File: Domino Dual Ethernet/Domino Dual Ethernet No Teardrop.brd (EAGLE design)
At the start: 38.1 x 30.5 mm, 29 parts, among them J1 MH10-1, J2 B50(27-51)FP4-151-A613-B12, J3 B50(27-51)FP4-151-A613-B12, J4 FR04-2, J5 FR04-1

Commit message: Changed copyright
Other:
- board text added: "Reference designs are provided "AS IS" and "WITH ALL FAULTS". The Domino Team disclaims all other warranties express or implied, regarding this product, including but not limited to, any implied warranties of merchantibility or fitness for any particular application."
- board text added: "The Domino Team may make changes to specifications and product descriptions at any time, without notice."
- board text added: "© 2014, The Domino Team. All rights reserved."
- board text removed: "Michel Stempin may make changes to specifications and product descriptions at any time, without notice."
- board text removed: "Reference designs are provided "AS IS" and "WITH ALL FAULTS". Michel Stempin disclaims all other warranties express or implied, regarding this product, including but not limited to, any implied warranties of merchantibility or fitness for any particular application."
- board text removed: "© 2014, Michel Stempin. All rights reserved."
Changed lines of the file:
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@@
 See creativecommons.org/licenses/by-sa/4.0/</text>
 <text x="34.29" y="-51.943" size="0.8128" layer="48" ratio="20">Reference designs are provided "AS IS" and "WITH ALL FAULTS".
-Michel Stempin disclaims all other warranties express or implied,
+The Domino Team disclaims all other warranties express or implied,
 regarding this product, including but not limited to, any implied warranties of
 merchantibility or fitness for any particular application.</text>
-<text x="34.29" y="-55.753" size="0.8128" layer="48" ratio="20">Michel Stempin may make changes to specifications and product descriptions
+<text x="34.29" y="-55.753" size="0.8128" layer="48" ratio="20">The Domino Team may make changes to specifications and product descriptions
 at any time, without notice.</text>
-<text x="74.93" y="-41.91" size="1.27" layer="48" ratio="20">© 2014, Michel Stempin.
+<text x="74.93" y="-41.91" size="1.27" layer="48" ratio="20">© 2014, The Domino Team.
 All rights reserved.</text>
 <text x="115.57" y="-57.15" size="1.778" layer="48">Rev.</text>

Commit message: Domino tile Dual Ethernet Revision B
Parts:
- removed J4: FR04-2, Domino:FR04-2-0.1
- removed J5: FR04-1, Domino:FR04-1-0.1
- added D1: BLUE, Domino:LED0603
- added D2: WHITE, Domino:LED0603
- added D3, D4, D5, D6: GREEN, Domino:LED0603
- added D7: RED, Domino:LED0603
- added D8: ORANGE, Domino:LED0603
- added D9: YELLOW, Domino:LED0603
- added R10, R11, R12, R13, R15: 270R, Domino:R0603
- added R14, R16: 150R, Domino:R0603
- added R17, R18: 330R, Domino:R0603
- added R9: 49R9, Domino:R0402
- added U$13: (no value), Domino:DOMINO_LOGO_SMALL
- added U$16: (no value), Domino:OPEN_HARDWARE_LOGO
- C1: device Domino:C1210 -> Domino:C1206
- J1: value MH10-1 -> B59(57-02)F4-03-1212-C12; device Domino:MH10-1-0.1 -> Domino:B59(57-02)F4-03-1212-C12
- J2, J3: value B50(27-51)FP4-151-A613-B12 -> MH18-1; device Domino:B50(27-51)FP4-151-A613-B12 -> Domino:MH18-1-0.1
- R1: value 49R9 -> 330R; device Domino:R0402 -> Domino:R0603
- moved J2 36.4 mm to (1.27, 31.8), flipped to the bottom, turned to 180 degrees
- moved U$4 32.8 mm to (39.4, 14.6), flipped to the bottom, turned to 270 degrees
- moved C5 26.3 mm to (29.0, 11.3), turned to 90 degrees
- moved R7 24.1 mm to (27.4, 22.1), flipped to the top
- moved R8 22.1 mm to (27.4, 17.7), flipped to the top, turned to 180 degrees
- moved U$7 22.1 mm to (30.5, 12.7)
- moved C6 21.5 mm to (29.0, 21.6), flipped to the top, turned to 270 degrees
- moved U$6 21.0 mm to (9.53, 3.17)
- moved C3 20.2 mm to (18.1, 5.32), flipped to the top, turned to 90 degrees
- moved U$8 19.3 mm to (15.9, 22.2)
- moved R5 18.5 mm to (27.4, 11.8), turned to 180 degrees
- moved C4 17.9 mm to (29.0, 14.7), flipped to the top
- moved U$5 14.5 mm to (17.8, 3.17)
- moved R6 14.4 mm to (27.4, 21.1)
- moved C1 14.3 mm to (15.5, 27.8), flipped to the top, turned to 180 degrees
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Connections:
- removed net P0_LED_L_A: J2.13, J4.8
- removed net P0_LED_L_C: J2.14, J4.7
- removed net P0_LED_R_A: J2.11, J4.4
- removed net P0_LED_R_C: J2.12, J4.3
- removed net P4_LED_L_A: J3.13, J4.6
- removed net P4_LED_L_C: J3.14, J4.5
- removed net P4_LED_R_A: J3.11, J4.2
- removed net P4_LED_R_C: J3.12, J4.1
- removed net VC12: J3.9, J5.3
- removed net VC36: J3.10, J5.4
- removed net VC45: J3.4, J5.1
- removed net VC78: J3.5, J5.2
- new net +3V3: D7.2, D8.2, D9.2, J1.UL2, J2.8, R1.2
- new net LAN1_LED: D3.2, R12.2
- new net LAN2_LED: D4.2, R13.2
- new net LAN3_LED: D5.2, J1.DL2, R14.2
- new net LAN4_LED: D6.2, R15.2
- new net LED0: J2.9, R10.1
- new net LED1: J2.10, R11.1
- new net LED2: J2.11, R12.1
- new net LED3: J2.12, R13.1
- new net LED4: J2.13, R14.1
- new net LED5: J2.14, R15.1
- new net LED6: J2.15, R16.1
- new net LED7: J2.16, R17.1
- new net LED8: J2.17, R18.1
- new net POWER_LED: J1.DL4, J1.UL4, R1.1
- new net SYS_LED: D8.1, R17.2
- new net USB_LED: D2.2, R11.2
- new net WAN_LED: D7.1, J1.UL1, R16.2
- new net WLAN_LED: D1.2, R10.2
- new net WPS_LED: D9.1, R18.2
- net +2VA_ETH_OUT: now also C2.2, C3.2, J1.DR2, J1.DR5, J1.UR2, J1.UR5, J3.14; no longer C6.2, C7.2, J1.6, J2.3, J3.3
- net GND: now also D1.1, D2.1, D3.1, D4.1, D5.1, D6.1, J1.DL1, J1.DL3, J1.UL3, J2.18, J3.9; no longer J1.1
- net P0_RX: now also C7.2, R8.1, R9.1; no longer C2.2, R1.1, R2.1
- net P0_RX_N: now also J1.DR3, J3.16, R9.2; no longer J1.8, J2.2, R2.2
- net P0_RX_P: now also J1.DR1, J3.15, R8.2; no longer J1.7, J2.1, R1.2
- net P0_TX: now also C6.2, R6.1, R7.1; no longer C3.2, R3.1, R4.1
- net P0_TX_N: now also J1.DR6, J3.18, R7.2; no longer J1.10, J2.8, R4.2
- net P0_TX_P: now also J1.DR4, J3.17, R6.2; no longer J1.9, J2.7, R3.2
- net P4_RX: now also C5.2, R4.1; no longer C4.2, R6.1
- net P4_RX_N: now also J1.UR6, J3.11, R5.2; no longer J1.3, J3.8, R6.2
- net P4_RX_P: now also J1.UR4, J3.10, R4.2; no longer J1.2, J3.7, R5.2
- net P4_TX: now also C4.2, R2.1, R3.1; no longer C5.2, R7.1, R8.1
- net P4_TX_N: now also J1.UR3, J3.13, R3.2; no longer J1.5, J3.2, R8.2
- net P4_TX_P: now also J1.UR1, J3.12, R2.2; no longer J1.4, J3.1, R7.2
- net SHIELD: now also J1.DR8, J1.P$1, J1.P$2, J1.P$3, J1.P$4, J1.UR8; no longer J2.6, J2.SH$1, J2.SH$2, J3.6, J3.SH$1, J3.SH$2
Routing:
- net +3V3: track 0.00 -> 56.1 mm, vias 0 -> 2
- net P4_LED_R_A: track 52.3 -> 0.00 mm
- net WAN_LED: track 0.00 -> 51.6 mm, vias 0 -> 1
- net P4_LED_R_C: track 47.2 -> 0.00 mm
- net LAN3_LED: track 0.00 -> 43.5 mm, vias 0 -> 1
- net P4_LED_L_A: track 41.9 -> 0.00 mm
- net P4_LED_L_C: track 36.5 -> 0.00 mm
- net +2VA_ETH_OUT: track 37.7 -> 74.0 mm
- net GND: track 0.00 -> 34.2 mm, vias 31 -> 57
- net P0_LED_R_A: track 32.3 -> 0.00 mm
- net POWER_LED: track 0.00 -> 31.1 mm, vias 0 -> 1
- net P0_LED_L_A: track 26.8 -> 0.00 mm
- net P0_LED_R_C: track 26.4 -> 0.00 mm
- net P0_TX_N: track 20.6 -> 47.0 mm, vias 0 -> 1
- net P0_LED_L_C: track 23.3 -> 0.00 mm
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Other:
- board size 38.1 x 30.5 mm -> 45.7 x 33 mm
- board text added: "+3V3"
- board text added: "7. SILKSCREEN BOARD USING BLACK INK. DISTORTION OF SILKSCREEN IS ACCEPTABLE OVER TRACES. EPOXY INK ON PLATED LANDS IS NOT ACCEPTABLE"
- board text added: "D1..9"
- board text added: "ELD2"
- board text added: "LAN1"
- board text added: "LAN2"
- board text added: "LAN3"
- board text added: "LAN4"
- board text added: "LED0"
- board text added: "LED1"
- board text added: "LED2"
- board text added: "LED3"
- board text added: "LED4"
- board text added: "LED5"
- board text added: "LED6"
- board text added: "LED7"
- board text added: "LED8"
- board text added: "P0 LAN"
- board text added: "P4 WAN"
- board text added: "R12..18"
- board text added: "SYS"
- board text added: "USB"
- board text added: "WLAN"
- board text added: "WPS"
- board text removed: "7. SILKSCREEN BOARD USING WHITE INK. DISTORTION OF SILKSCREEN IS ACCEPTABLE OVER TRACES. EPOXY INK ON PLATED LANDS IS NOT ACCEPTABLE"
- board text removed: "LAN"
- board text removed: "LEDS"
- board text removed: "P0"
- board text removed: "P0_LED_L"
- board text removed: "P0_LED_R"
- board text removed: "P0_RX+"
- board text removed: "P0_RX-"
- board text removed: "P0_TX+"
- board text removed: "P0_TX-"
- board text removed: "P4"
- board text removed: "P4_LED_L"
- board text removed: "P4_LED_R"
- board text removed: "PoE"
- board text removed: "Rev. A"
- board text removed: "VC12"
- board text removed: "VC36"
- board text removed: "VC45"
- board text removed: "VC78"
- board text removed: "_A"
- board text removed: "_C"

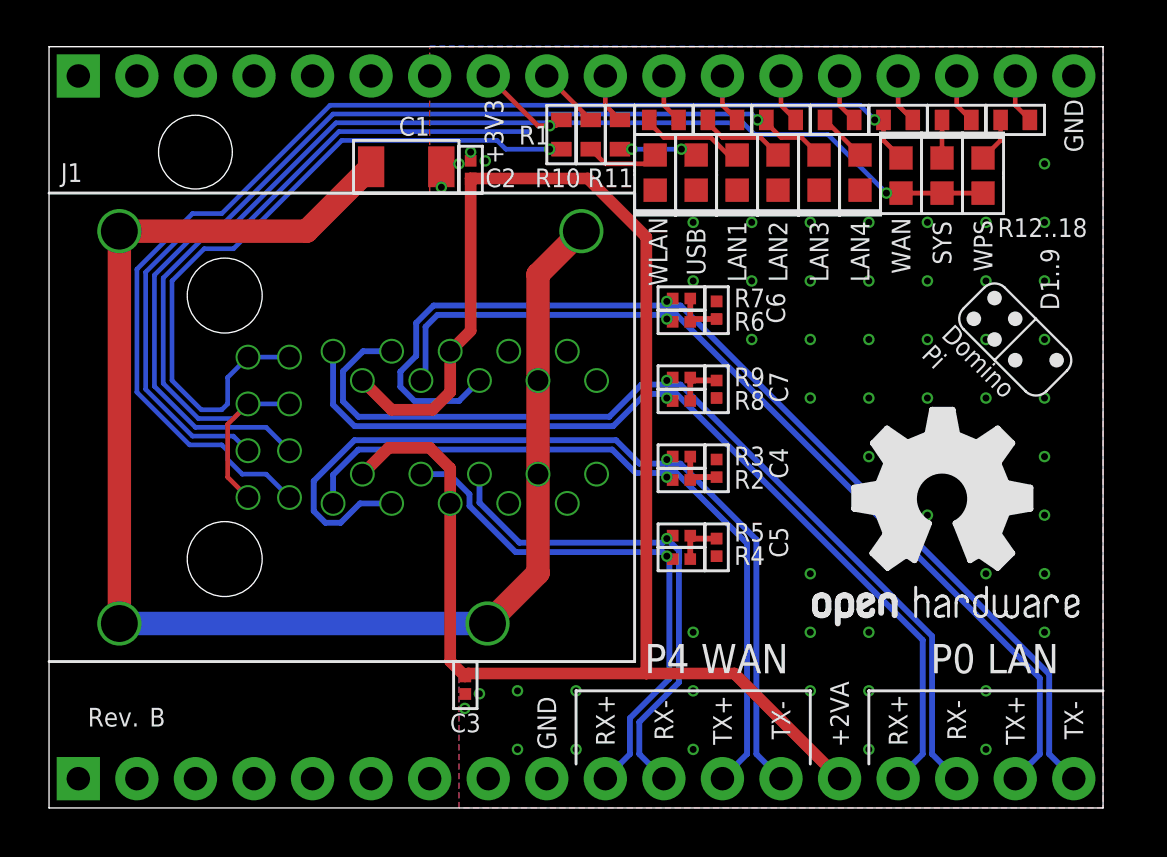
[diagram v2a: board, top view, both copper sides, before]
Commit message: Domino Single USB tile Revision B
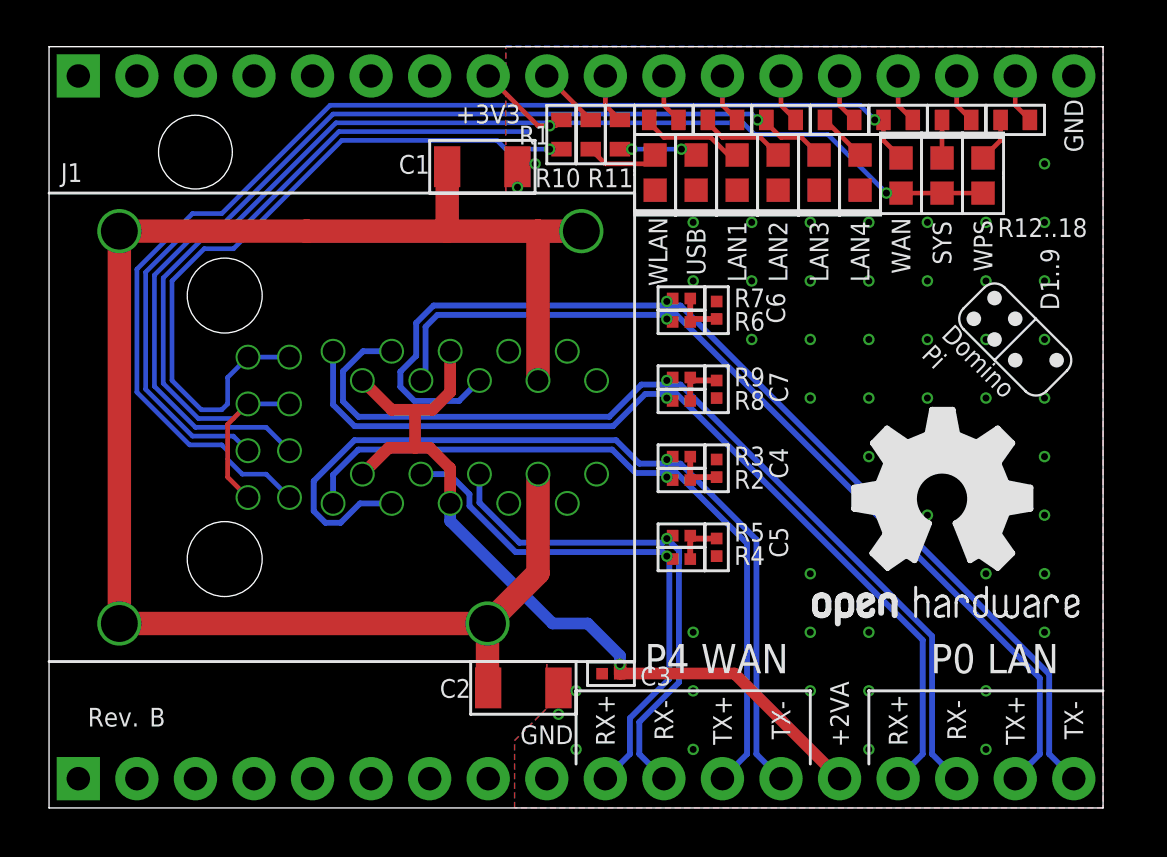
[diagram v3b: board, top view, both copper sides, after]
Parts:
- C2: value 100n -> 2n2; device Domino:C0402 -> Domino:C1206
- moved C2 22.6 mm to (20.6, 5.21), turned to 180 degrees
- moved C3 6.34 mm to (24.4, 5.82), turned to 0 degrees
- moved C1 3.30 mm to (18.8, 27.8)
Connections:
- net +2VA_ETH_OUT: no longer C2.2
- net SHIELD: now also C2.2
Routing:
- net +2VA_ETH_OUT: track 74.0 -> 37.4 mm, vias 0 -> 1
- net SHIELD: track 63.8 -> 72.5 mm
- net GND: vias 57 -> 52

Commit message: Replaced RJ45 Jack with one model without LED in Dual Ethernet tile
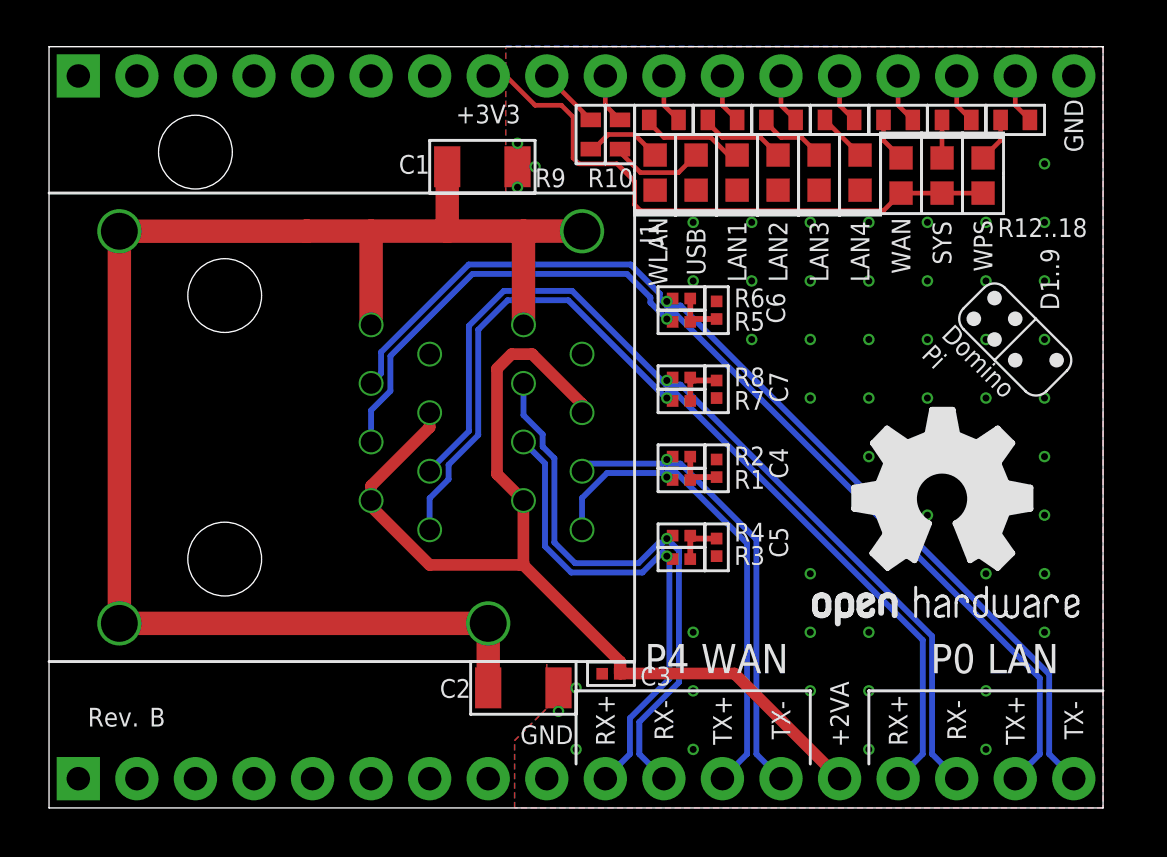
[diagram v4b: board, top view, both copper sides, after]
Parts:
- removed R18: 330R, Domino:R0603
- J1: value B59(57-02)F4-03-1212-C12 -> HL-59T-2X1; device Domino:B59(57-02)F4-03-1212-C12 -> Domino:HL-59T-2X1
- R1: value 330R -> 49R9; device Domino:R0603 -> Domino:R0402
- R14: value 150R -> 270R
- R15: value 270R -> 330R
- R16: value 150R -> 330R
- R9: value 49R9 -> 270R; device Domino:R0402 -> Domino:R0603
- moved R1 15.9 mm to (27.4, 14.2), turned to 180 degrees
- moved U$8 13.5 mm to (5.71, 13.3)
- moved R9 11.3 mm to (23.5, 29.2), turned to 270 degrees
- moved R5 9.27 mm to (27.4, 21.1)
- moved R3 4.45 mm to (27.4, 10.8)
- moved R7 4.45 mm to (27.4, 17.7)
- moved R12 2.54 mm to (29.2, 29.8)
- moved R13 2.54 mm to (31.8, 29.8)
- moved R14 2.54 mm to (34.3, 29.8)
- moved R15 2.54 mm to (36.8, 29.8)
- moved R16 2.54 mm to (39.4, 29.8)
- moved R17 2.54 mm to (41.9, 29.8)
- moved R11 2.01 mm to (26.7, 29.8), turned to 180 degrees
- moved R10 1.27 mm to (24.8, 29.2)
- moved R8 1.02 mm to (27.4, 18.7)
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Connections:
- removed net POWER_LED: J1.DL4, J1.UL4, R1.1
- net +2VA_ETH_OUT: now also J1.DP2, J1.DP5, J1.UP2, J1.UP5; no longer J1.DR2, J1.DR5, J1.UR2, J1.UR5
- net +3V3: no longer J1.UL2, R1.2
- net GND: no longer J1.DL1, J1.DL3, J1.UL3
- net LAN1_LED: now also R11.2; no longer R12.2
- net LAN2_LED: now also R12.2; no longer R13.2
- net LAN3_LED: now also R13.2; no longer J1.DL2, R14.2
- net LAN4_LED: now also R14.2; no longer R15.2
- net LED0: now also R9.1; no longer R10.1
- net LED1: now also R10.1; no longer R11.1
- net LED2: now also R11.1; no longer R12.1
- net LED3: now also R12.1; no longer R13.1
- net LED4: now also R13.1; no longer R14.1
- net LED5: now also R14.1; no longer R15.1
- net LED6: now also R15.1; no longer R16.1
- net LED7: now also R16.1; no longer R17.1
- net LED8: now also R17.1; no longer R18.1
- net P0_RX: now also R7.1; no longer R9.1
- net P0_RX_N: now also J1.DP3, R8.2; no longer J1.DR3, R9.2
- net P0_RX_P: now also J1.DP1, R7.2; no longer J1.DR1, R8.2
- net P0_TX: now also R5.1; no longer R7.1
- net P0_TX_N: now also J1.DP6, R6.2; no longer J1.DR6, R7.2
- net P0_TX_P: now also J1.DP4, R5.2; no longer J1.DR4, R6.2
- net P4_RX: now also R3.1; no longer R5.1
- net P4_RX_N: now also J1.UP6, R4.2; no longer J1.UR6, R5.2
- net P4_RX_P: now also J1.UP4, R3.2; no longer J1.UR4, R4.2
- net P4_TX: now also R1.1; no longer R3.1
- net P4_TX_N: now also J1.UP3, R2.2; no longer J1.UR3, R3.2
- net P4_TX_P: now also J1.UP1, R1.2; no longer J1.UR1, R2.2
- net SHIELD: now also J1.DP8, J1.UP8; no longer J1.DR8, J1.UR8
- net SYS_LED: now also R16.2; no longer R17.2
- net USB_LED: now also R10.2; no longer R11.2
- net WAN_LED: now also R15.2; no longer J1.UL1, R16.2
- net WLAN_LED: now also R9.2; no longer R10.2
- net WPS_LED: now also R17.2; no longer R18.2
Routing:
- net WAN_LED: track 51.6 -> 1.97 mm, vias 1 -> 0
- net LAN3_LED: track 43.5 -> 2.99 mm, vias 1 -> 0
- net GND: track 34.2 -> 0.00 mm, vias 52 -> 53
- net POWER_LED: track 31.1 -> 0.00 mm, vias 1 -> 0
- net +3V3: track 56.1 -> 25.8 mm, vias 2 -> 0
- net P4_TX_N: track 38.3 -> 20.4 mm
- net P4_TX_P: track 32.5 -> 21.5 mm
- net +2VA_ETH_OUT: track 37.4 -> 45.4 mm, vias 1 -> 0
- net SHIELD: track 72.5 -> 66.8 mm
- net P0_TX_P: track 41.1 -> 46.5 mm
- net P4_RX_N: track 22.3 -> 25.2 mm
- net P0_RX_P: track 40.2 -> 42.5 mm
- net P0_TX_N: track 47.0 -> 45.0 mm
- net P4_RX_P: track 23.6 -> 22.3 mm
- net P0_RX_N: track 41.8 -> 41.0 mm
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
